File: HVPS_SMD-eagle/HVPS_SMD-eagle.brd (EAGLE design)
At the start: 40.6 x 25.7 mm, 17 parts, among them Q1 DMT10H010LK3, T1 749196141, U1 LM3478MM/NOPB

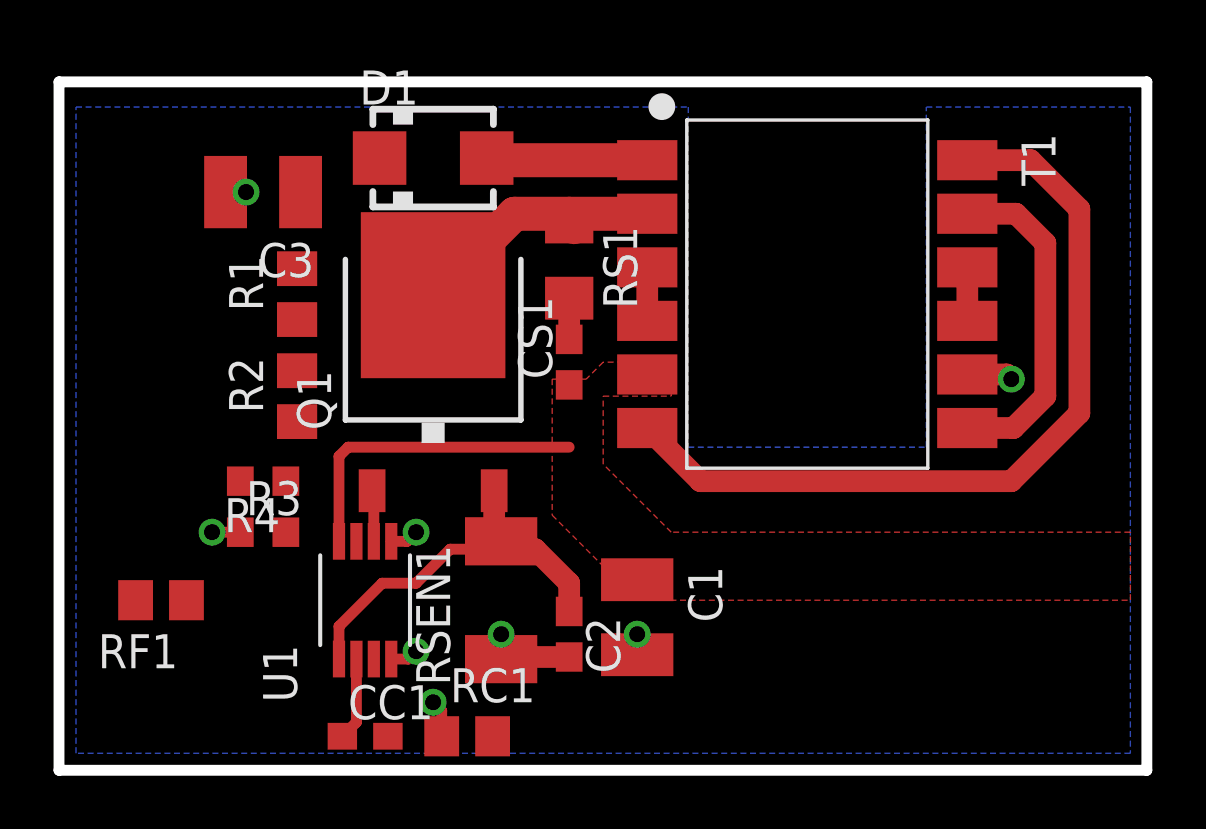
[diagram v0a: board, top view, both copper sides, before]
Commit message: -Completed layout. -Added headers.
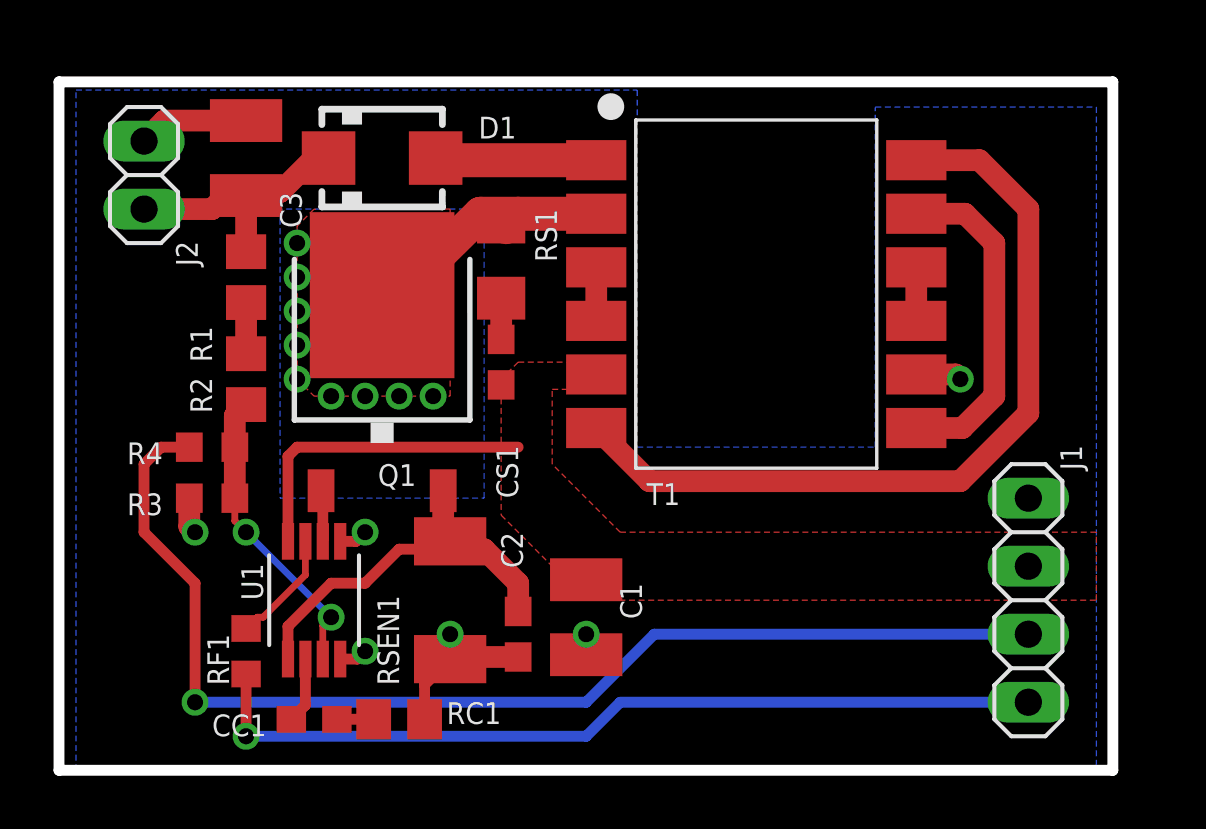
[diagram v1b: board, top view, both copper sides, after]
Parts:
- added J1: (no value), pinhead:1X04
- added J2: (no value), pinhead:1X02
- RF1: value 47K -> 10K; device rcl:R0805 -> rcl:R0603
- moved RF1 3.70 mm to (6.99, 4.45), turned to 270 degrees
- moved RC1 2.62 mm to (12.7, 1.91), turned to 180 degrees
- moved CS1 2.54 mm to (16.5, 15.2)
- moved RS1 2.54 mm to (16.5, 19.1)
- moved R3 2.29 mm to (5.71, 10.2)
- moved R4 2.29 mm to (5.71, 12.1)
- moved R2 2.01 mm to (6.99, 14.6)
- moved CC1 2.01 mm to (9.53, 1.91)
- moved R1 2.01 mm to (6.99, 18.4)
- moved C1 1.91 mm to (19.7, 5.71)
- moved C2 1.91 mm to (17.1, 5.08)
- moved D1 1.91 mm to (12.1, 22.9)
- moved Q1 1.91 mm to (12.1, 15.2)
- moved RSEN1 1.91 mm to (14.6, 6.35)
- moved T1 1.91 mm to (26.0, 17.8)
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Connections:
- net N$5 renamed Q_DRAIN
- net EN: now also J1.4
- net GND: now also J1.1, J2.1
- net V+: now also J1.2
- net VADJ: now also J1.3
- net VOUT: now also J2.2
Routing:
- net VADJ: track 0.00 -> 43.8 mm, vias 0 -> 1
- net EN: track 0.00 -> 32.1 mm, vias 0 -> 1
- net FB: track 0.00 -> 11.3 mm, vias 0 -> 2
- net VOUT: track 0.00 -> 9.77 mm
- net GND: track 11.3 -> 16.2 mm, vias 8 -> 6
- net N$1: track 0.00 -> 4.30 mm
- net Q_DRAIN: track 9.83 -> 13.6 mm, vias 0 -> 9
- net N$14: track 0.00 -> 1.91 mm
- net N$3: track 0.00 -> 1.38 mm
- net N$2: track 3.10 -> 2.47 mm
- added copper zone on layer 1, net Q_DRAIN
- added copper zone on layer 16, net Q_DRAIN
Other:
- board size 40.6 x 25.7 mm -> 39.4 x 25.7 mm
- board text added: "!! 200V OUT !!"
- board text added: "+++"
- board text added: "---"
- board text added: "3V-12V"
- board text added: "EN"
- board text added: "GND"
- board text added: "VADJ"

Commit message: -Reduced via drills. -Silkscreen cleanup. -Revision A.
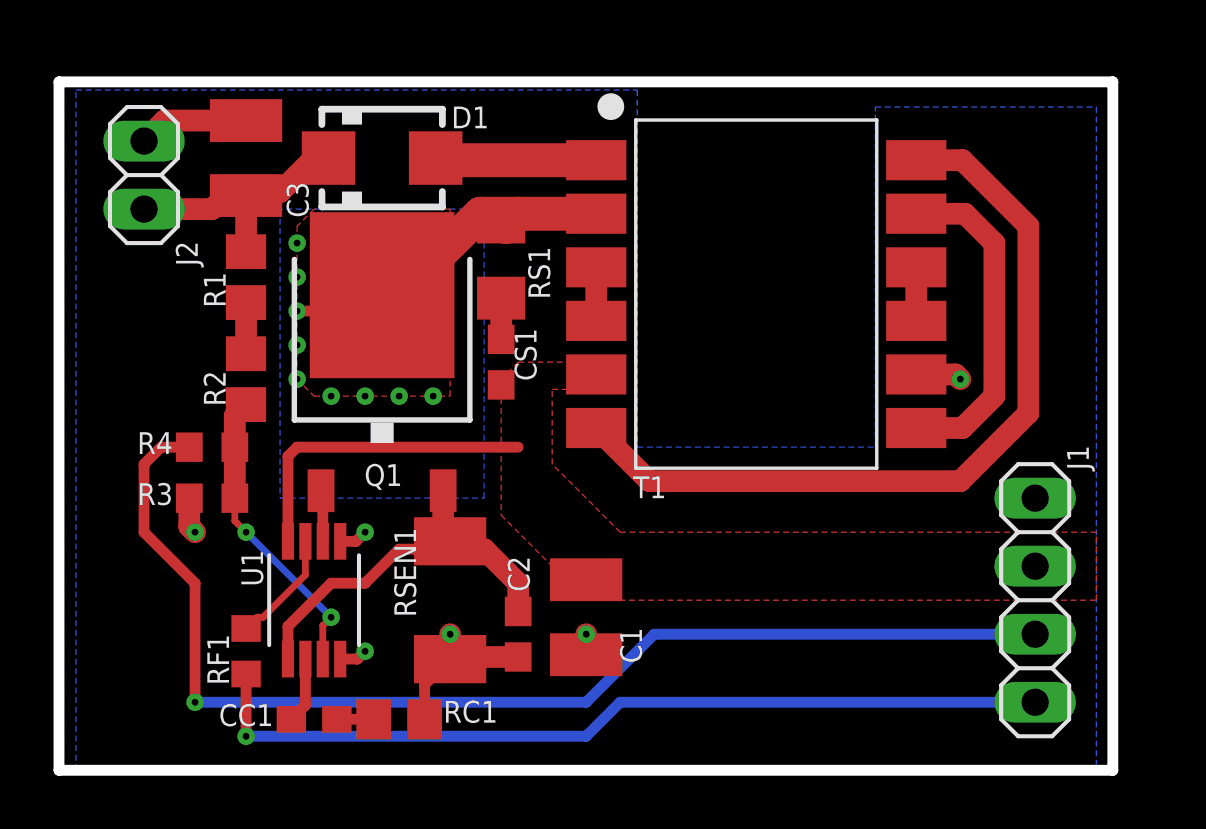
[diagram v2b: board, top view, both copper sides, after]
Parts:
- moved J1 0.25 mm to (36.4, 6.35)
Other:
- board text added: ">DRAWING_NAME"
- board text added: "Rev A"

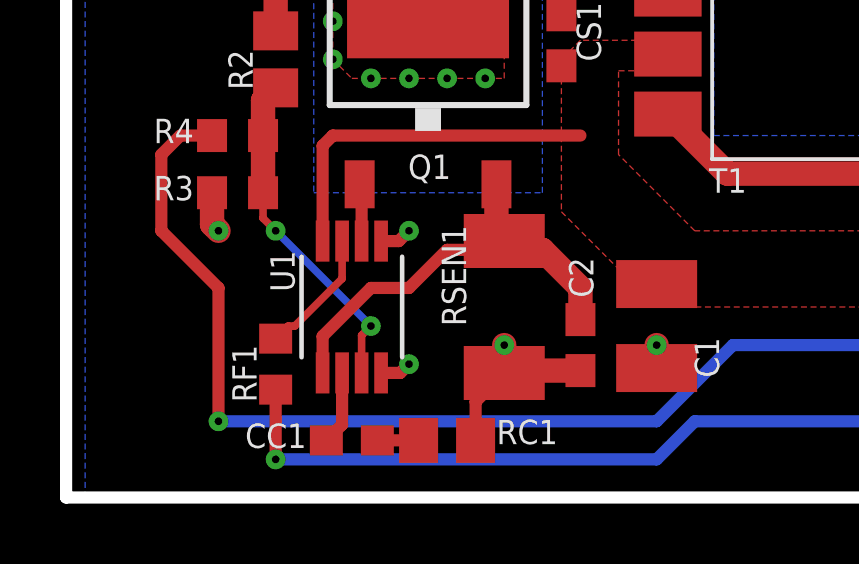
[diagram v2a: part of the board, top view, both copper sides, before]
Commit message: -Updated design rules. -Added proper FA/SD signal path.
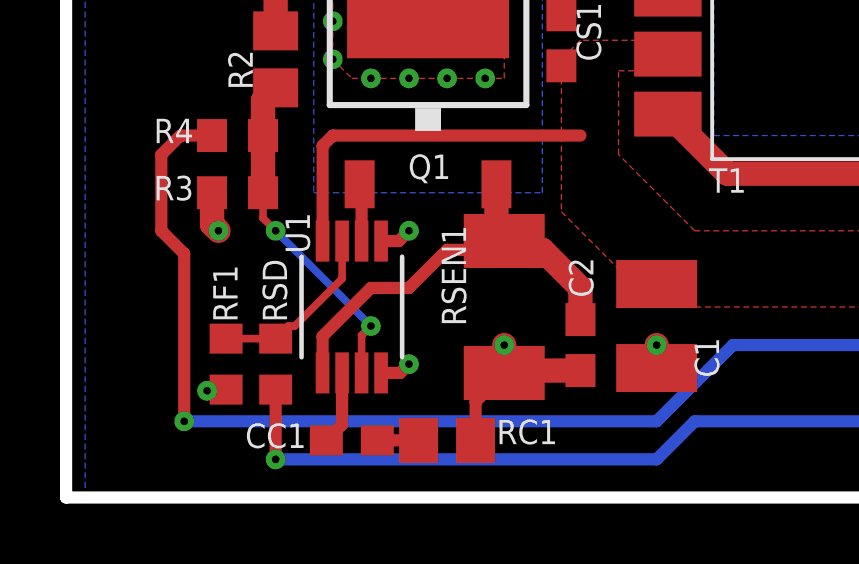
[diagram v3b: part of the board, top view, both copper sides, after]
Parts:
- added RSD: 10K, rcl:R0603
- RF1: value 10K -> 47K
- moved RF1 1.65 mm to (5.33, 4.45), turned to 90 degrees
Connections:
- removed net EN: J1.4, RF1.2
- new net SD: J1.4, RSD.2
- net GND: now also RF1.1
- net N$1: now also RF1.2, RSD.1; no longer RF1.1
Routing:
- net SD: track 0.00 -> 32.3 mm, vias 0 -> 1
- net EN: track 32.3 -> 0.00 mm, vias 1 -> 0
- net N$1: track 4.30 -> 5.95 mm
- net GND: track 16.2 -> 16.9 mm, vias 6 -> 7
- net VADJ: track 44.1 -> 44.7 mm
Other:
- board text added: "SD"
- board text removed: "EN"
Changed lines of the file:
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@@
 <setting verticaltext="up"/>
 </settings>
-<grid distance="0.05" unitdist="inch" unit="inch" style="lines" multiple="1" display="no" altdistance="0.01" altunitdist="inch" altunit="inch"/>
+<grid distance="0.05" unitdist="inch" unit="inch" style="lines" multiple="1" display="no" altdistance="0.005" altunitdist="inch" altunit="inch"/>
 <layers>
 <layer number="1" name="Top" color="4" fill="1" visible="yes" active="yes"/>
@@
 <layer number="45" name="Holes" color="7" fill="1" visible="no" active="yes"/>
 <layer number="46" name="Milling" color="3" fill="1" visible="no" active="yes"/>
-<layer number="47" name="Measures" color="7" fill="1" visible="no" active="yes"/>
+<layer number="47" name="Measures" color="7" fill="1" visible="yes" active="yes"/>
 <layer number="48" name="Document" color="7" fill="1" visible="yes" active="yes"/>
 <layer number="49" name="Reference" color="7" fill="1" visible="no" active="yes"/>
@@
 <wire x1="39.35" y1="25.705" x2="0" y2="25.705" width="0.4064" layer="20"/>
 <wire x1="0" y1="25.705" x2="0" y2="0" width="0.4064" layer="20"/>
-<text x="34.29" y="3.175" size="0.8128" layer="48" rot="R180">EN</text>
+<text x="34.29" y="3.175" size="0.8128" layer="48" rot="R180">SD</text>
 <text x="34.29" y="5.715" size="0.8128" layer="48" rot="R180">VADJ</text>
 <text x="34.29" y="8.255" size="0.8128" layer="48" rot="R180">3V-12V</text>
@@
 <text x="19.685" y="1.905" size="0.8128" layer="48">&gt;DRAWING_NAME</text>
 <text x="19.685" y="0.635" size="0.8128" layer="48">Rev A</text>
+<dimension x1="0" y1="25.705" x2="0" y2="0" x3="-2.54" y3="12.8525" textsize="0.8128" layer="47" dtype="vertical"/>
+<dimension x1="39.35" y1="25.705" x2="0" y2="25.705" x3="19.675" y3="27.94" textsize="0.8128" layer="47" dtype="vertical"/>
 </plain>
 <attributes>
@@
 <param name="mdSmdStop" value="0mil"/>
 <param name="msWidth" value="6mil"/>
-<param name="msDrill" value="12mil"/>
+<param name="msDrill" value="10mil"/>
 <param name="msMicroVia" value="9.99mm"/>
 <param name="msBlindViaRatio" value="0.5"/>
@@
 <attribute name="VALUE" x="13.335" y="4.445" size="0.8128" layer="27" rot="R180"/>
 </element>
-<element name="RF1" library="rcl" package="R0603" value="10K" x="6.985" y="4.445" smashed="yes" rot="R270">
-<attribute name="NAME" x="6.35" y="3.175" size="0.8128" layer="25" rot="R90"/>
+<element name="RSD" library="rcl" package="R0603" value="10K" x="6.985" y="4.445" smashed="yes" rot="R270">
+<attribute name="NAME" x="7.366" y="5.842" size="0.8128" layer="25" rot="R90"/>
 <attribute name="VALUE" x="5.08" y="5.08" size="0.8128" layer="27" rot="R270"/>
 </element>
@@
 <attribute name="VENDOR" value="Texas Instruments" x="9.525" y="6.35" size="1.778" layer="27" rot="R90" display="off"/>
 <attribute name="MANUFACTURER_PART_NUMBER" value="LM3478MMNOPB" x="9.525" y="6.35" size="1.778" layer="27" rot="R90" display="off"/>
-<attribute name="NAME" x="7.62" y="6.858" size="0.8128" layer="25" ratio="6" rot="SR90"/>
+<attribute name="NAME" x="8.128" y="8.128" size="0.8128" layer="25" ratio="6" rot="SR90"/>
 <attribute name="VALUE" x="13.335" y="2.54" size="0.8128" layer="27" ratio="6" rot="R90"/>
 </element>
@@
 <attribute name="VALUE" x="33.274" y="11.43" size="1.27" layer="27" rot="R270"/>
 </element>
+<element name="RF1" library="rcl" package="R0603" value="47K" x="5.334" y="4.445" smashed="yes" rot="R90">
+<attribute name="NAME" x="5.715" y="5.842" size="0.8128" layer="25" rot="R90"/>
+<attribute name="VALUE" x="7.239" y="3.81" size="1.27" layer="27" rot="R90"/>
+</element>
 </elements>
 <signals>
 <signal name="N$1">
-<contactref element="RF1" pad="1"/>
+<contactref element="RSD" pad="1"/>
 <contactref element="U1" pad="7"/>
 <wire x1="9.2" y1="8.5471" x2="9.2" y2="7.295" width="0.254" layer="1"/>
@@
 <wire x1="7.62" y1="5.715" x2="7.405" y2="5.715" width="0.254" layer="1"/>
 <wire x1="7.405" y1="5.715" x2="6.985" y2="5.295" width="0.254" layer="1"/>
-</signal>
-<signal name="EN">
 <contactref element="RF1" pad="2"/>
+<wire x1="5.334" y1="5.295" x2="6.985" y2="5.295" width="0.254" layer="1"/>
+</signal>
+<signal name="SD">
+<contactref element="RSD" pad="2"/>
 <contactref element="J1" pad="4"/>
 <wire x1="6.985" y1="3.595" x2="6.985" y2="1.27" width="0.4064" layer="1"/>
@@
 <wire x1="13.65" y1="1.905" x2="13.65" y2="3.195" width="0.4064" layer="1"/>
 <wire x1="13.65" y1="3.195" x2="14.605" y2="4.15" width="0.4064" layer="1"/>
+<contactref element="RF1" pad="1"/>
+<wire x1="5.334" y1="3.595" x2="4.699" y2="3.595" width="0.254" layer="1"/>
+<wire x1="4.699" y1="3.595" x2="4.699" y2="3.556" width="0.254" layer="1"/>
+<via x="4.699" y="3.556" extent="1-16" drill="0.254"/>
 </signal>
 <signal name="FB">
@@
 <wire x1="3.81" y1="12.065" x2="3.175" y2="11.43" width="0.4064" layer="1"/>
 <wire x1="3.175" y1="11.43" x2="3.175" y2="8.89" width="0.4064" layer="1"/>
-<wire x1="3.175" y1="8.89" x2="5.08" y2="6.985" width="0.4064" layer="1"/>
-<wire x1="5.08" y1="6.985" x2="5.08" y2="2.54" width="0.4064" layer="1"/>
-<via x="5.08" y="2.54" extent="1-16" drill="0.254" diameter="0.4064"/>
-<wire x1="5.08" y1="2.54" x2="19.685" y2="2.54" width="0.4064" layer="16"/>
+<wire x1="3.175" y1="8.89" x2="3.937" y2="8.128" width="0.4064" layer="1"/>
+<wire x1="3.937" y1="8.128" x2="3.937" y2="2.54" width="0.4064" layer="1"/>
+<via x="3.937" y="2.54" extent="1-16" drill="0.254" diameter="0.4064"/>
+<wire x1="3.937" y1="2.54" x2="19.685" y2="2.54" width="0.4064" layer="16"/>
 <wire x1="19.685" y1="2.54" x2="22.225" y2="5.08" width="0.4064" layer="16"/>
 <wire x1="22.225" y1="5.08" x2="36.449" y2="5.08" width="0.4064" layer="16"/>
